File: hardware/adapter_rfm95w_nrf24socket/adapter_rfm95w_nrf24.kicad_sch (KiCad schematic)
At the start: 4 parts, among them J1 Conn_02x04_Odd_Even, J2 Conn_01x01, J3 Conn_01x01, J4 Conn_01x07

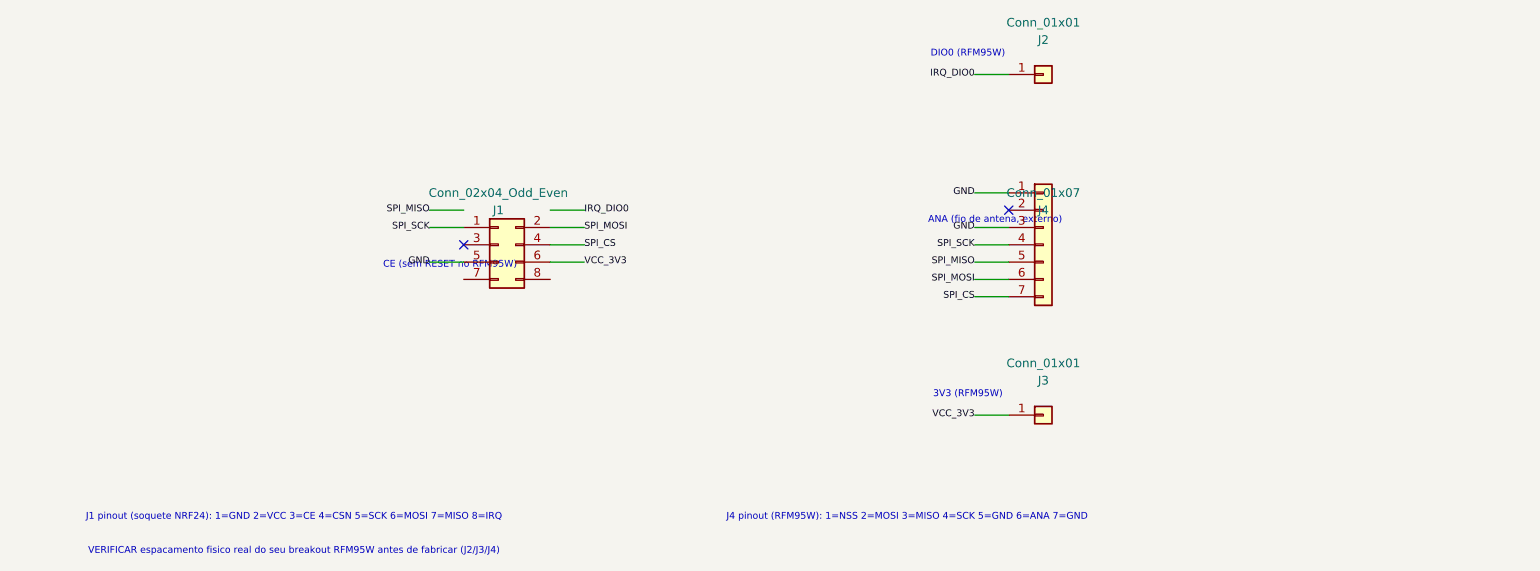
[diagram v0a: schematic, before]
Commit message: feat: add KiCad design for RFM95W to NRF24 socket adapter
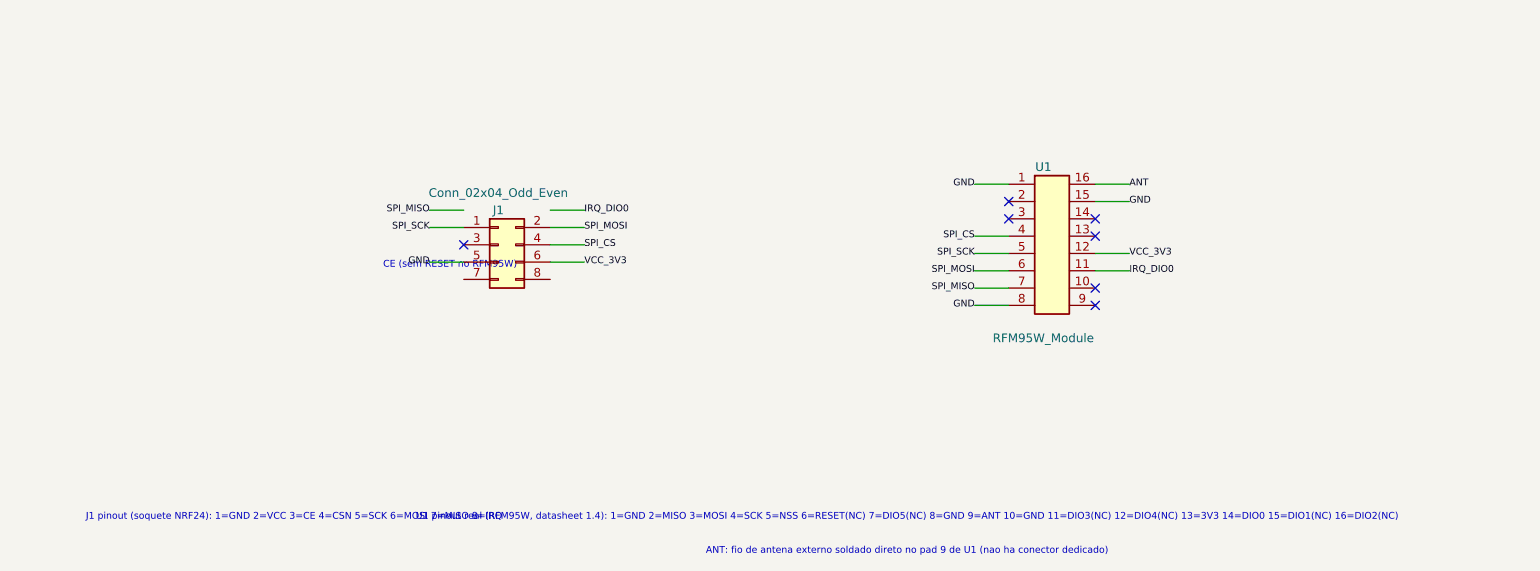
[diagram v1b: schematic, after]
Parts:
- removed J2, J3: Conn_01x01, Connector_PinHeader_2.54mm:PinHeader_1x01_P2.54mm_Vertical, symbol Connector_Generic:Conn_01x01
- removed J4: Conn_01x07, Connector_PinHeader_2.54mm:PinHeader_1x07_P2.54mm_Vertical, symbol Connector_Generic:Conn_01x07
- added U1: RFM95W_Module, M360_RFM95W:RFM95W_SMD_16P, symbol M360_RFM95W:RFM95W_Module
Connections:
- net GND: now also U1.1 (GND), U1.15 (DIO1), U1.8 (GND)
- net IRQ_DIO0: now also U1.11 (DIO3)
- net SPI_CS: now also U1.4 (SCK)
- net SPI_MISO: now also U1.7 (DIO5)
- net SPI_MOSI: now also U1.6 (RESET)
- net SPI_SCK: now also U1.5 (NSS)
- net VCC_3V3: now also U1.12 (DIO4)
- new net ANT: U1.16 (DIO2)
- no-connect marks 2 -> 7
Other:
- note added: "ANT: fio de antena externo soldado direto no pad 9 de U1 (nao ha conector dedicado)"
- note added: "U1 pinout real (RFM95W, datasheet 1.4): 1=GND 2=MISO 3=MOSI 4=SCK 5=NSS 6=RESET(NC) 7=DIO5(NC) 8=GND 9=ANT 10=GND 11=DIO3(NC) 12=DIO4(NC) 13=3V3 14=DIO0 15=DIO1(NC) 16=DIO2(NC)"
- note removed: "3V3 (RFM95W)"
- note removed: "ANA (fio de antena, externo)"
- note removed: "DIO0 (RFM95W)"
- note removed: "J4 pinout (RFM95W): 1=NSS 2=MOSI 3=MISO 4=SCK 5=GND 6=ANA 7=GND"
- note removed: "VERIFICAR espacamento fisico real do seu breakout RFM95W antes de fabricar (J2/J3/J4)"
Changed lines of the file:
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@@
     (title "Adaptador NRF24 Socket -> RFM95W breakout")
     (date "2026-07-04")
-    (rev "A")
+    (rev "C")
     (company "M360 Horta")
-    (comment 1 "Pluga no soquete 2x4 originalmente para NRF24L01+ (placa YL-105 com AMS1117 + level shifter)")
-    (comment 2 "Alimenta e conecta um breakout RFM95W (pinout: NSS,MOSI,MISO,SCK,GND,ANA,GND + DIO0 + 3V3)")
-    (comment 3 "CE do soquete NRF24 fica sem ligacao: este breakout RFM95W nao expoe pino RESET")
+    (comment 1 "J1 (2x4 THT) pluga direto no soquete da placa YL-105 (NRF24L01+, AMS1117 + level shifter)")
+    (comment 2 "U1 usa o footprint real do RFM95W (16 pads castelados, 16x16mm, pitch 2mm - datasheet Fig.56)")
+    (comment 3 "CE (J1) e RESET/DIO5/DIO3/DIO4/DIO1/DIO2 (U1) ficam sem ligacao, conforme solicitado")
   )
   (no_connect (at 54.92 90))
-  (no_connect (at 134.92 84.92))
+  (no_connect (at 134.92 86.19))
+  (no_connect (at 134.92 83.65))
+  (no_connect (at 147.62 86.19))
+  (no_connect (at 147.62 88.73))
+  (no_connect (at 147.62 96.35))
+  (no_connect (at 147.62 98.89))
   (wire (pts (xy 54.92 92.54) (xy 49.92 92.54))
     (stroke (width 0))
@@
     (stroke (width 0))
   )
-  (wire (pts (xy 134.92 65) (xy 129.92 65))
+  (wire (pts (xy 134.92 98.89) (xy 129.92 98.89))
     (stroke (width 0))
   )
-  (wire (pts (xy 134.92 115) (xy 129.92 115))
+  (wire (pts (xy 134.92 96.35) (xy 129.92 96.35))
     (stroke (width 0))
   )
-  (wire (pts (xy 134.92 97.62) (xy 129.92 97.62))
+  (wire (pts (xy 134.92 93.81) (xy 129.92 93.81))
     (stroke (width 0))
   )
-  (wire (pts (xy 134.92 95.08) (xy 129.92 95.08))
+  (wire (pts (xy 134.92 91.27) (xy 129.92 91.27))
     (stroke (width 0))
   )
-  (wire (pts (xy 134.92 92.54) (xy 129.92 92.54))
+  (wire (pts (xy 134.92 88.73) (xy 129.92 88.73))
     (stroke (width 0))
   )
-  (wire (pts (xy 134.92 90.0) (xy 129.92 90.0))
+  (wire (pts (xy 134.92 81.11) (xy 129.92 81.11))
     (stroke (width 0))
   )
-  (wire (pts (xy 134.92 87.46) (xy 129.92 87.46))
+  (wire (pts (xy 147.62 81.11) (xy 152.62 81.11))
     (stroke (width 0))
   )
-  (wire (pts (xy 134.92 82.38) (xy 129.92 82.38))
+  (wire (pts (xy 147.62 83.65) (xy 152.62 83.65))
+    (stroke (width 0))
+  )
+  (wire (pts (xy 147.62 91.27) (xy 152.62 91.27))
+    (stroke (width 0))
+  )
+  (wire (pts (xy 147.62 93.81) (xy 152.62 93.81))
     (stroke (width 0))
   )
   (text "CE (sem RESET no RFM95W)" (at 52.92 93 0)
-    (effects (font (size 1.0 1.0)))
-  )
-  (text "DIO0 (RFM95W)" (at 128.92 62 0)
-    (effects (font (size 1.0 1.0)))
-  )
-  (text "3V3 (RFM95W)" (at 128.92 112 0)
-    (effects (font (size 1.0 1.0)))
-  )
-  (text "ANA (fio de antena, externo)" (at 132.92 86.42 0)
-    (effects (font (size 1.0 1.0)))
-  )
-  (text "J4 pinout (RFM95W): 1=NSS 2=MOSI 3=MISO 4=SCK 5=GND 6=ANA 7=GND"
-    (at 120 130 0)
     (effects (font (size 1.0 1.0)))
   )
@@
     (effects (font (size 1.0 1.0)))
   )
-  (text "VERIFICAR espacamento fisico real do seu breakout RFM95W antes de fabricar (J2/J3/J4)"
-    (at 30 135 0)
+  (text "U1 pinout real (RFM95W, datasheet 1.4): 1=GND 2=MISO 3=MOSI 4=SCK 5=NSS 6=RESET(NC) 7=DIO5(NC) 8=GND 9=ANT 10=GND 11=DIO3(NC) 12=DIO4(NC) 13=3V3 14=DIO0 15=DIO1(NC) 16=DIO2(NC)"
+    (at 120 130 0)
+    (effects (font (size 1.0 1.0)))
+  )
+  (text "ANT: fio de antena externo soldado direto no pad 9 de U1 (nao ha conector dedicado)"
+    (at 120 135 0)
     (effects (font (size 1.0 1.0)))
   )
@@
     (effects (font (size 1.0 1.0)))
   )
-  (label "IRQ_DIO0" (at 129.92 65 180)
+  (label "GND" (at 129.92 98.89 180)
     (effects (font (size 1.0 1.0)))
   )
-  (label "VCC_3V3" (at 129.92 115 180)
+  (label "SPI_MISO" (at 129.92 96.35 180)
     (effects (font (size 1.0 1.0)))
   )
-  (label "SPI_CS" (at 129.92 97.62 180)
+  (label "SPI_MOSI" (at 129.92 93.81 180)
     (effects (font (size 1.0 1.0)))
   )
-  (label "SPI_MOSI" (at 129.92 95.08 180)
+  (label "SPI_SCK" (at 129.92 91.27 180)
     (effects (font (size 1.0 1.0)))
   )
-  (label "SPI_MISO" (at 129.92 92.54 180)
+  (label "SPI_CS" (at 129.92 88.73 180)
     (effects (font (size 1.0 1.0)))
   )
-  (label "SPI_SCK" (at 129.92 90.0 180)
+  (label "GND" (at 129.92 81.11 180)
     (effects (font (size 1.0 1.0)))
   )
-  (label "GND" (at 129.92 87.46 180)
+  (label "ANT" (at 152.62 81.11 0)
     (effects (font (size 1.0 1.0)))
   )
-  (label "GND" (at 129.92 82.38 180)
+  (label "GND" (at 152.62 83.65 0)
+    (effects (font (size 1.0 1.0)))
+  )
+  (label "VCC_3V3" (at 152.62 91.27 0)
+    (effects (font (size 1.0 1.0)))
+  )
+  (label "IRQ_DIO0" (at 152.62 93.81 0)
     (effects (font (size 1.0 1.0)))
   )
@@
     (pin "8")
   )
-  (symbol (lib_id "Connector_Generic:Conn_01x01") (at 140 65) (unit 1)
+  (symbol (lib_id "M360_RFM95W:RFM95W_Module") (at 140 90) (unit 1)
     (in_bom yes) (on_board yes)
-    (property "Reference" "J2" (at 140 59.92 0)
+    (property "Reference" "U1" (at 140 78.57 0)
       (effects (font (size 1.27 1.27)))
     )
-    (property "Value" "Conn_01x01" (at 140 57.38 0)
+    (property "Value" "RFM95W_Module" (at 140 103.7 0)
       (effects (font (size 1.27 1.27)))
     )
-    (property "Footprint" "Connector_PinHeader_2.54mm:PinHeader_1x01_P2.54mm_Vertical" (at 140 65 0)
-      (effects (font (size 1.27 1.27)) hide)
-    )
-    (property "Datasheet" "~" (at 140 65 0)
-      (effects (font (size 1.27 1.27)) hide)
-    )
-    (pin "1")
-  )
-  (symbol (lib_id "Connector_Generic:Conn_01x01") (at 140 115) (unit 1)
-    (in_bom yes) (on_board yes)
-    (property "Reference" "J3" (at 140 109.92 0)
-      (effects (font (size 1.27 1.27)))
-    )
-    (property "Value" "Conn_01x01" (at 140 107.38 0)
-      (effects (font (size 1.27 1.27)))
-    )
-    (property "Footprint" "Connector_PinHeader_2.54mm:PinHeader_1x01_P2.54mm_Vertical" (at 140 115 0)
-      (effects (font (size 1.27 1.27)) hide)
-    )
-    (property "Datasheet" "~" (at 140 115 0)
-      (effects (font (size 1.27 1.27)) hide)
-    )
-    (pin "1")
-  )
-  (symbol (lib_id "Connector_Generic:Conn_01x07") (at 140 90) (unit 1)
-    (in_bom yes) (on_board yes)
-    (property "Reference" "J4" (at 140 84.92 0)
-      (effects (font (size 1.27 1.27)))
-    )
-    (property "Value" "Conn_01x07" (at 140 82.38 0)
-      (effects (font (size 1.27 1.27)))
-    )
-    (property "Footprint" "Connector_PinHeader_2.54mm:PinHeader_1x07_P2.54mm_Vertical" (at 140 90 0)
+    (property "Footprint" "M360_RFM95W:RFM95W_SMD_16P" (at 140 90 0)
       (effects (font (size 1.27 1.27)) hide)
     )
@@
     (pin "6")
     (pin "7")
+    (pin "8")
+    (pin "9")
+    (pin "10")
+    (pin "11")
+    (pin "12")
+    (pin "13")
+    (pin "14")
+    (pin "15")
+    (pin "16")
   )
 )
